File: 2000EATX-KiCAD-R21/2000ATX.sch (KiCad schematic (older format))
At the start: 0 parts

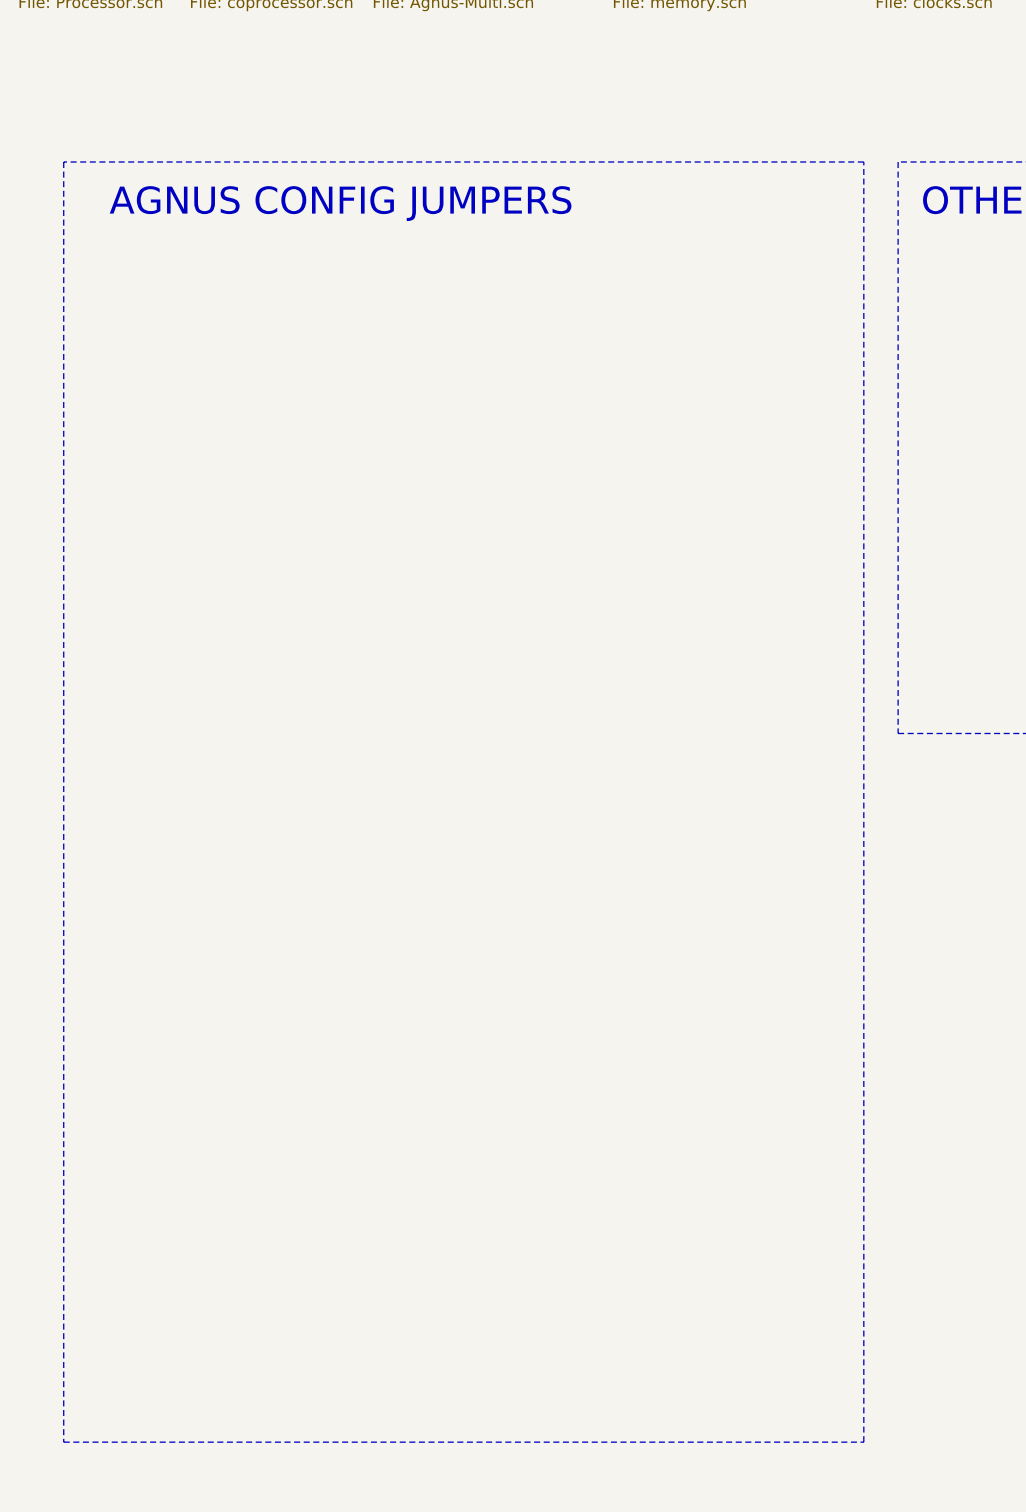
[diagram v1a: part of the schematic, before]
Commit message: Update Rev 2.1 KiCad Agnus Configuration Jumpers
Update the agnus configuration jumper tables in the schematics and on the board.
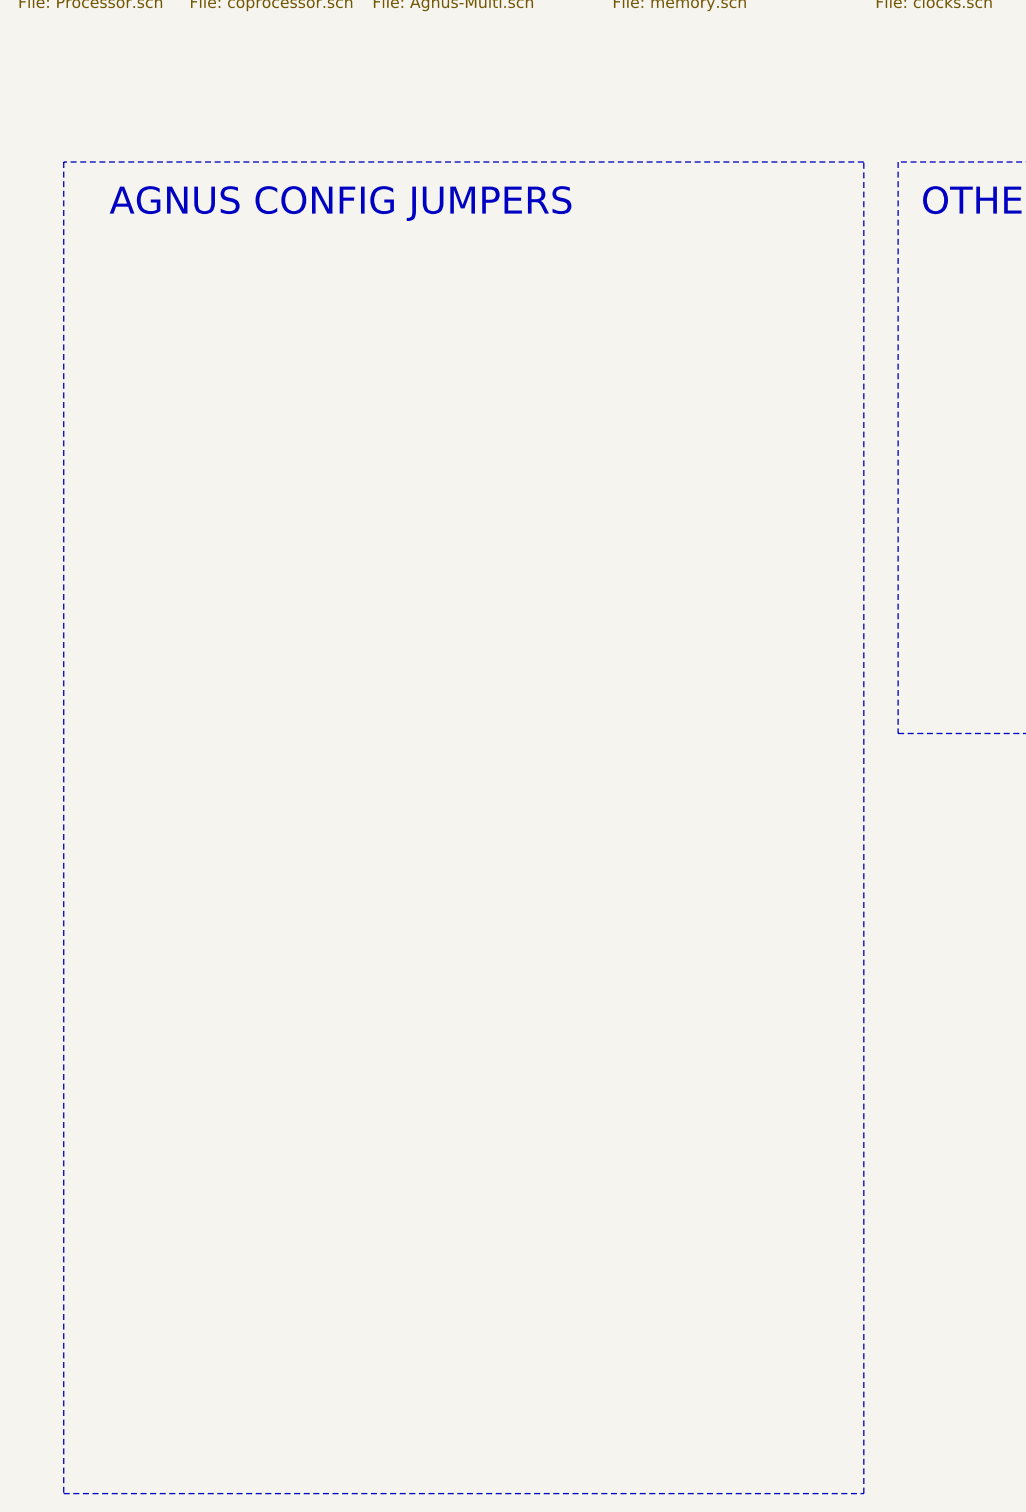
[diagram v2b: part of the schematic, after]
